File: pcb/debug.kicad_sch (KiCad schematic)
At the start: 9 parts, among them J5 TC2030, J6 CNC_Tech_3220-14-0100-00

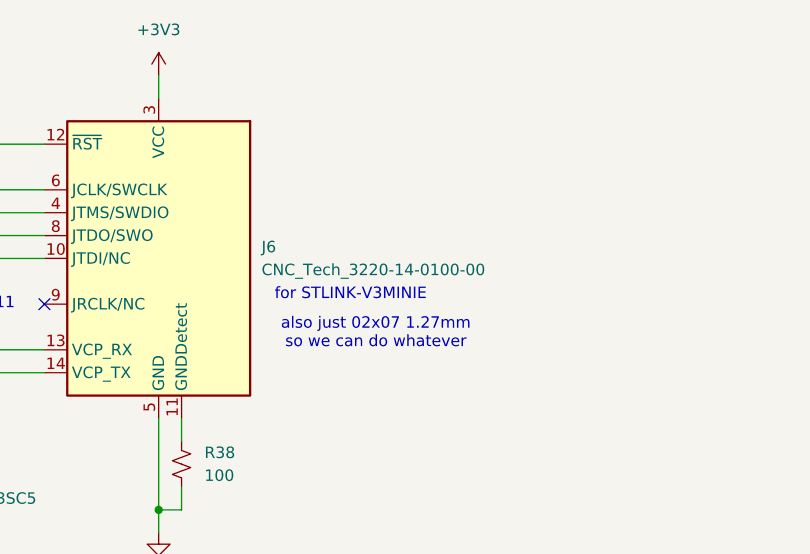
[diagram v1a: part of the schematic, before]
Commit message: Add MPN field for components except resistors
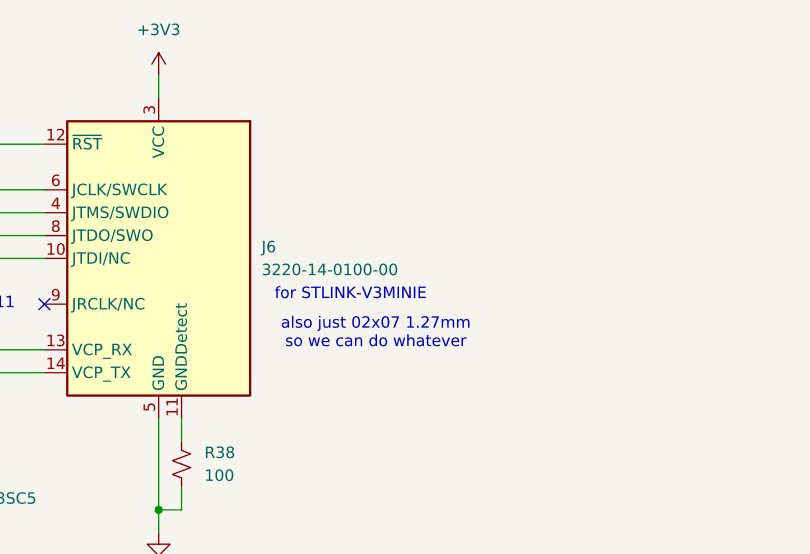
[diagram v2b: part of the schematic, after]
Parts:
- D6, D7: MPN (none) -> ESDA5V3SC5
- J6: value CNC_Tech_3220-14-0100-00 -> 3220-14-0100-00; MPN (none) -> 3220-14-0100-00
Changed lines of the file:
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@@
 			)
 		)
-		(property "Value" "CNC_Tech_3220-14-0100-00"
+		(property "Value" "3220-14-0100-00"
 			(at 125.73 44.4499 0)
 			(effects
@@
 		)
 		(property "Description" "ST Debug Connector, standard ARM Cortex-M SWD and JTAG interface plus UART"
+			(at 114.3 43.18 0)
+			(effects
+				(font
+					(size 1.27 1.27)
+				)
+				(hide yes)
+			)
+		)
+		(property "MPN" "3220-14-0100-00"
 			(at 114.3 43.18 0)
 			(effects
@@
 			)
 		)
+		(property "MPN" ""
+			(at 116.84 66.04 0)
+			(effects
+				(font
+					(size 1.27 1.27)
+				)
+				(hide yes)
+			)
+		)
 		(pin "2"
 		)
@@
 			)
 		)
+		(property "MPN" ""
+			(at 45.72 152.4 0)
+			(effects
+				(font
+					(size 1.27 1.27)
+				)
+				(hide yes)
+			)
+		)
 		(pin "1"
 		)
@@
 		)
 		(property "Description" "Quad TVS Diode Array, 5.3V Standoff, 4 Channels, 400W, ±30kV, SOT-23-5"
+			(at 55.88 68.58 0)
+			(effects
+				(font
+					(size 1.27 1.27)
+				)
+				(hide yes)
+			)
+		)
+		(property "MPN" "ESDA5V3SC5"
 			(at 55.88 68.58 0)
 			(effects
@@
 			)
 		)
+		(property "MPN" ""
+			(at 45.72 165.1 0)
+			(effects
+				(font
+					(size 1.27 1.27)
+				)
+				(hide yes)
+			)
+		)
 		(pin "1"
 		)
@@
 			)
 		)
+		(property "MPN" ""
+			(at 45.72 146.05 0)
+			(effects
+				(font
+					(size 1.27 1.27)
+				)
+				(hide yes)
+			)
+		)
 		(pin "2"
 		)
@@
 			)
 		)
+		(property "MPN" ""
+			(at 45.72 158.75 0)
+			(effects
+				(font
+					(size 1.27 1.27)
+				)
+				(hide yes)
+			)
+		)
 		(pin "2"
 		)
@@
 		)
 		(property "Description" "Quad TVS Diode Array, 5.3V Standoff, 4 Channels, 400W, ±30kV, SOT-23-5"
+			(at 81.28 68.58 0)
+			(effects
+				(font
+					(size 1.27 1.27)
+				)
+				(hide yes)
+			)
+		)
+		(property "MPN" "ESDA5V3SC5"
 			(at 81.28 68.58 0)
 			(effects
@@
 			(at 107.95 172.72 0)
 			(effects
+				(font
+					(size 1.27 1.27)
+				)
+				(hide yes)
+			)
+		)
+		(property "MPN" ""
+			(at 107.95 172.72 0)
+			(effects

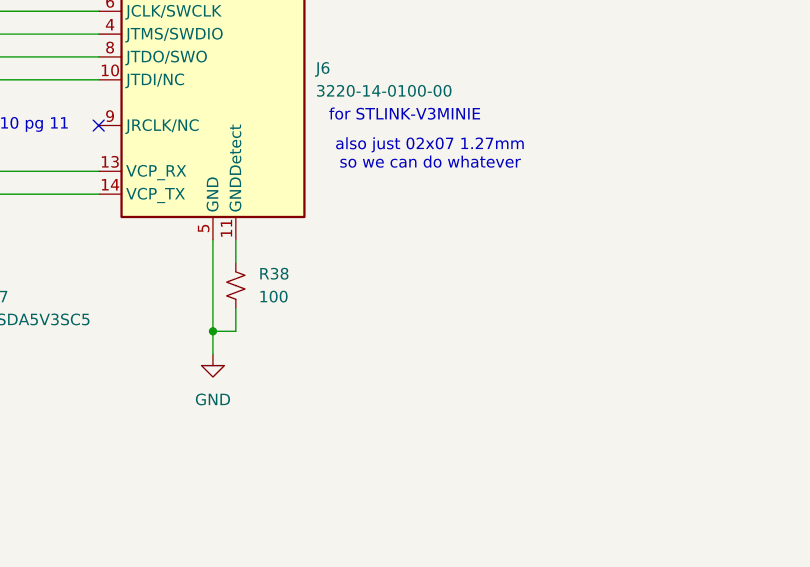
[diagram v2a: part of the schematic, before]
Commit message: BOM optimize 100 ohm resistors to 150 ohm
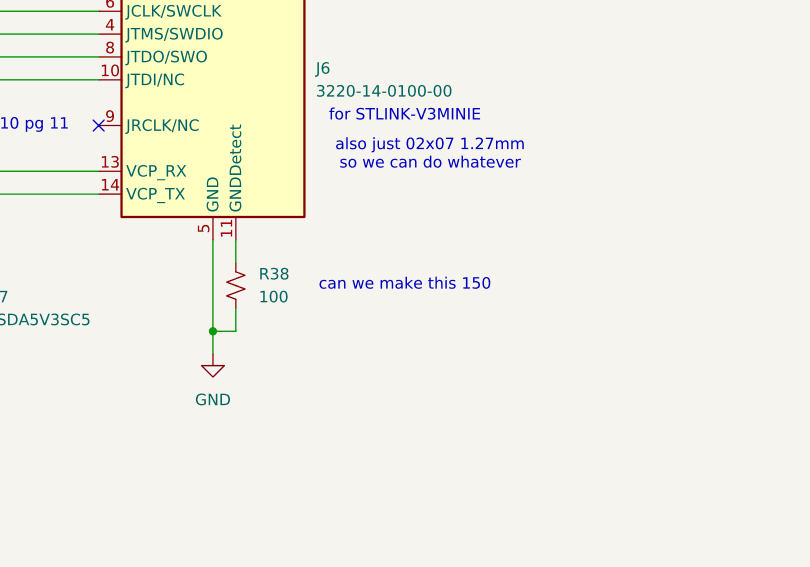
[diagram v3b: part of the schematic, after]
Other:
- note added: "can we make this 150"
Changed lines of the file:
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@@
+		)
+	)
+	(text "can we make this 150"
+		(exclude_from_sim no)
+		(at 135.636 66.04 0)
+		(effects
+			(font
+				(size 1.27 1.27)
+			)
 		)
 	)

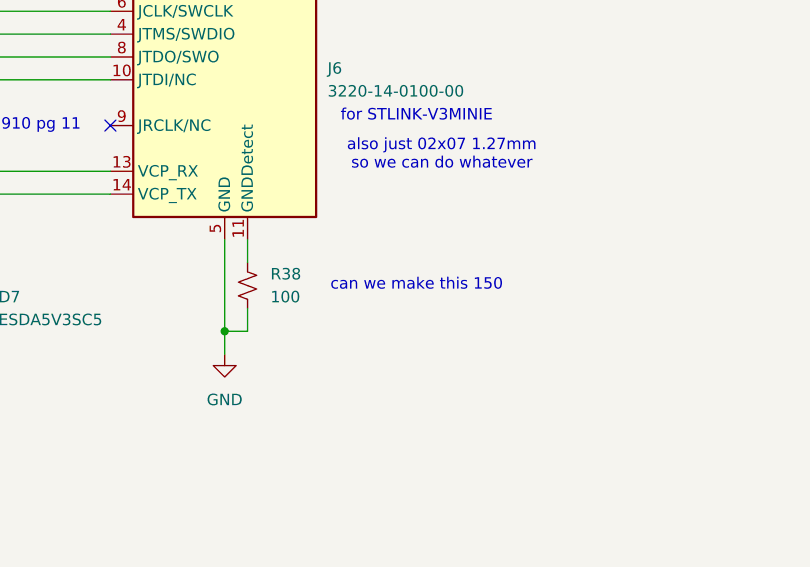
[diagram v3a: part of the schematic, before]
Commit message: BOM optimize GNDDetect 100 ohm resistor to 150 ohm
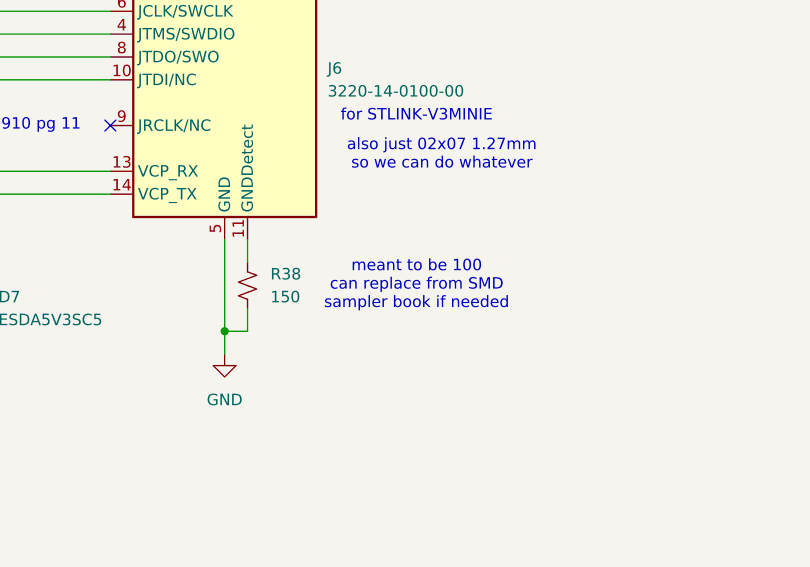
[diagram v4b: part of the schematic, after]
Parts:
- R38: value 100 -> 150
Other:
- note added: "meant to be 100 can replace from SMD sampler book if needed"
- note removed: "can we make this 150"
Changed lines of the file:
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@@
 		)
 	)
-	(text "can we make this 150"
+	(text "meant to be 100\ncan replace from SMD\nsampler book if needed"
 		(exclude_from_sim no)
 		(at 135.636 66.04 0)
@@
 			)
 		)
-		(property "Value" "100"
+		(property "Value" "150"
 			(at 119.38 67.3099 0)
 			(effects

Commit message: Update resistor MPNs
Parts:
- R38: MPN (none) -> RC0603JR-07150RL
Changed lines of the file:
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@@
 			)
 		)
-		(property "MPN" ""
+		(property "MPN" "RC0603JR-07150RL"
 			(at 116.84 66.04 0)
 			(effects

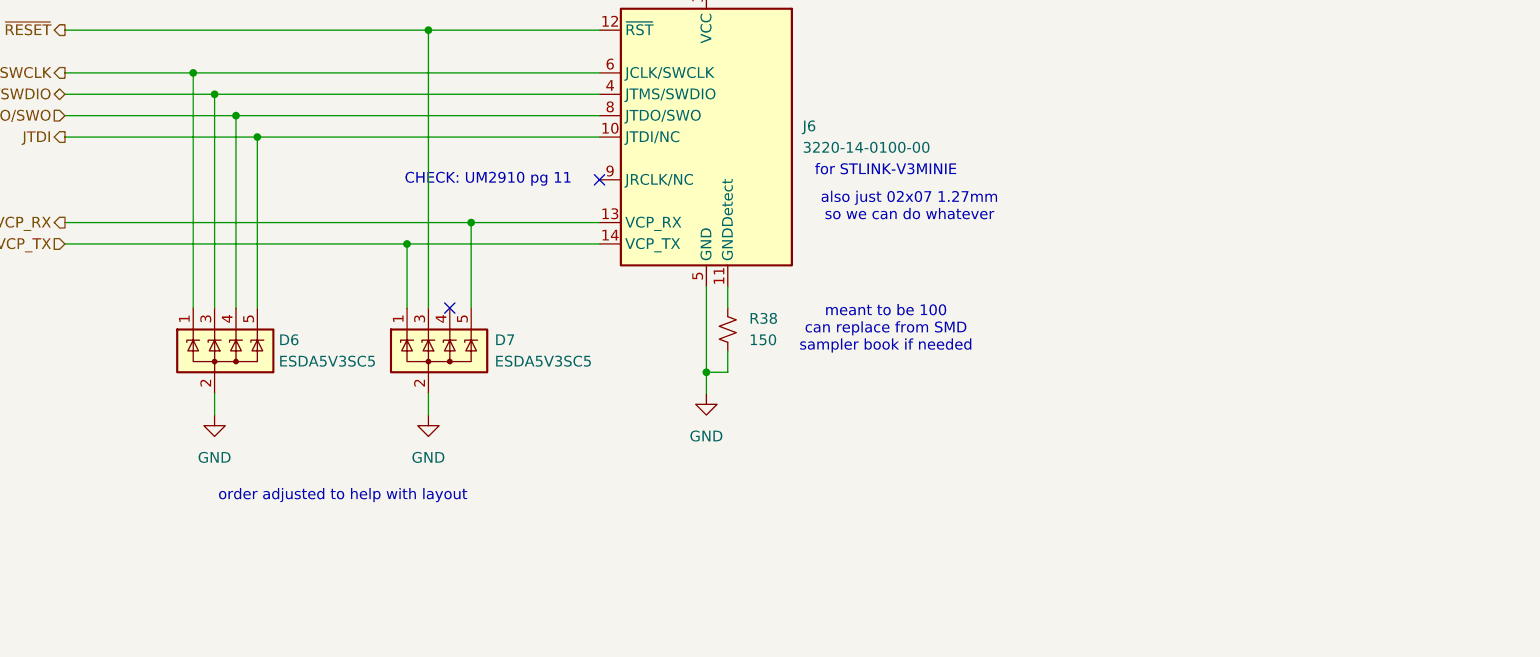
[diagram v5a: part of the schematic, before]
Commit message: Cleanup alex black eyes page
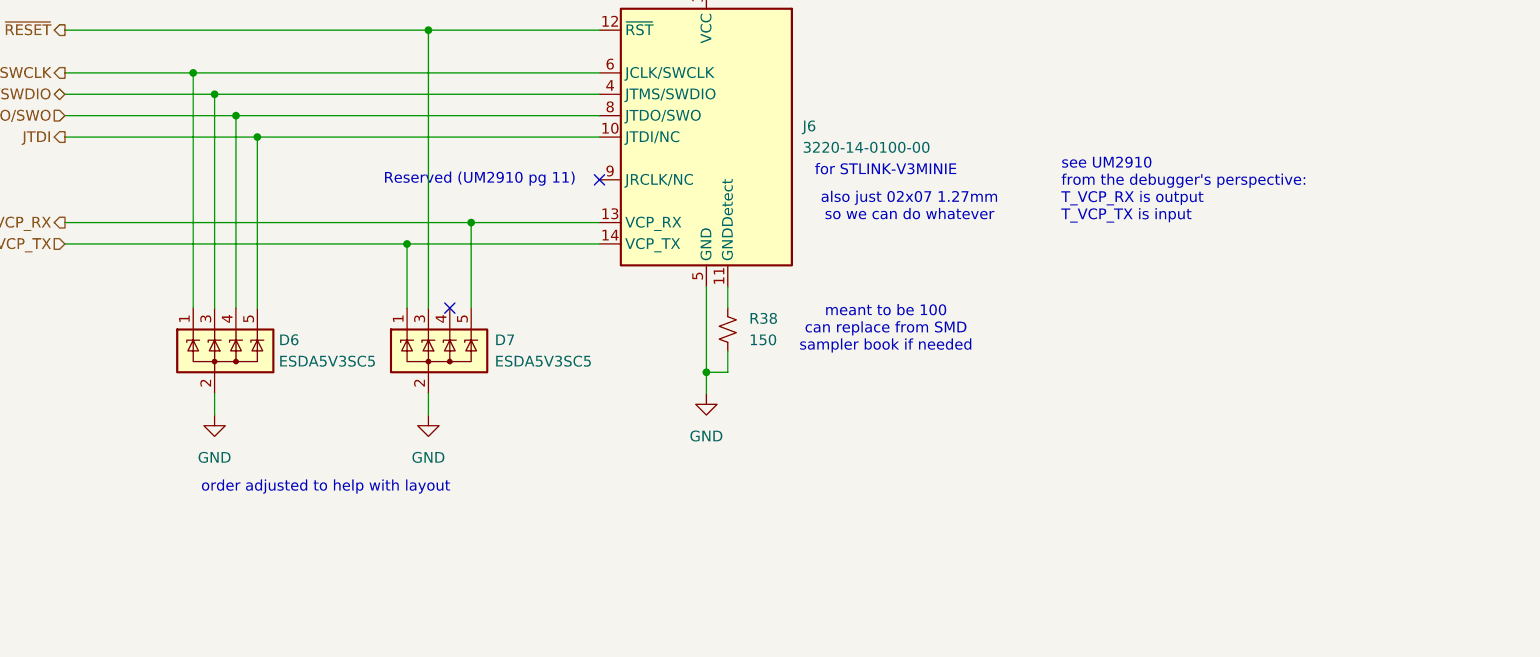
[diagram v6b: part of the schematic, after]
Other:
- note added: "Reserved (UM2910 pg 11)"
- note added: "see UM2910 from the debugger's perspective: T_VCP_RX is output T_VCP_TX is input"
- note removed: "CHECK: UM2910 pg 11"
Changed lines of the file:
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@@
 	(text "order adjusted to help with layout"
 		(exclude_from_sim no)
-		(at 71.12 85.852 0)
+		(at 69.088 84.836 0)
 		(effects
 			(font
 				(size 1.27 1.27)
 			)
+		)
+	)
+	(text "see UM2910\nfrom the debugger's perspective:\nT_VCP_RX is output\nT_VCP_TX is input"
+		(exclude_from_sim no)
+		(at 156.464 45.72 0)
+		(effects
+			(font
+				(size 1.27 1.27)
+			)
+			(justify left top)
 		)
 	)
@@
 		)
 	)
-	(text "CHECK: UM2910 pg 11"
+	(text "Reserved (UM2910 pg 11)"
 		(exclude_from_sim no)
-		(at 88.392 48.26 0)
+		(at 87.376 48.26 0)
 		(effects
 			(font

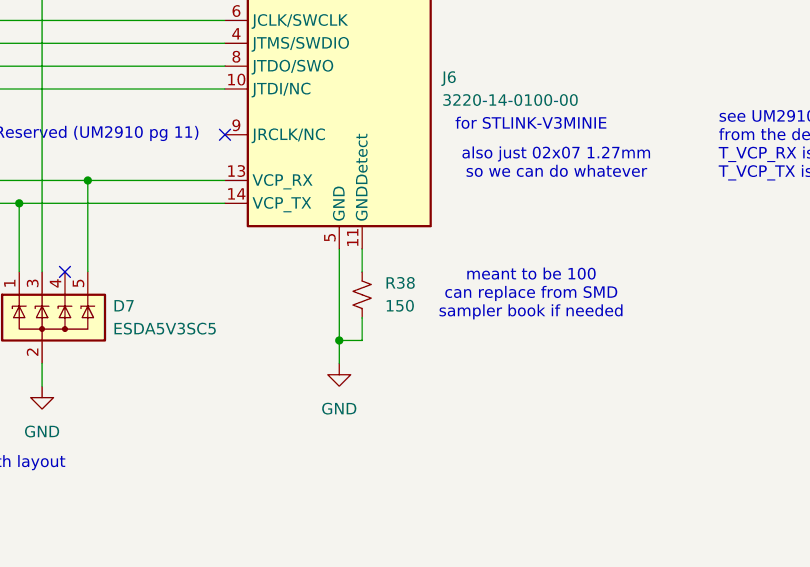
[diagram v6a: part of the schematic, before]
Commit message: Redo layout and routing for RGB LEDs
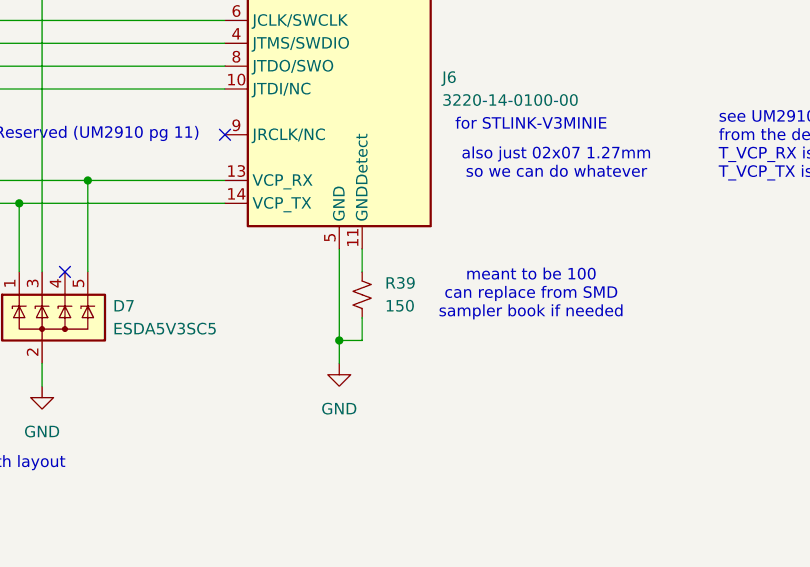
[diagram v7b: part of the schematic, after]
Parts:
- renumbered R38 to R39

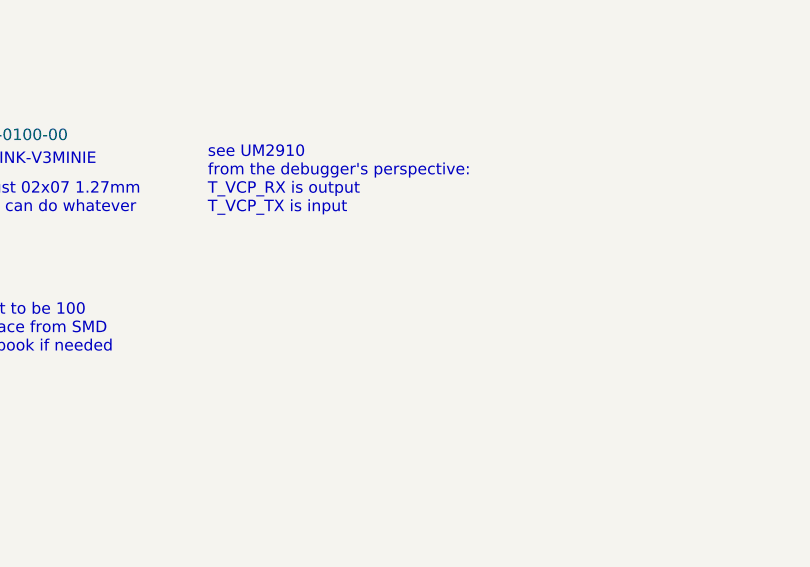
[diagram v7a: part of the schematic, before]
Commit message: Plot schematics for tech report
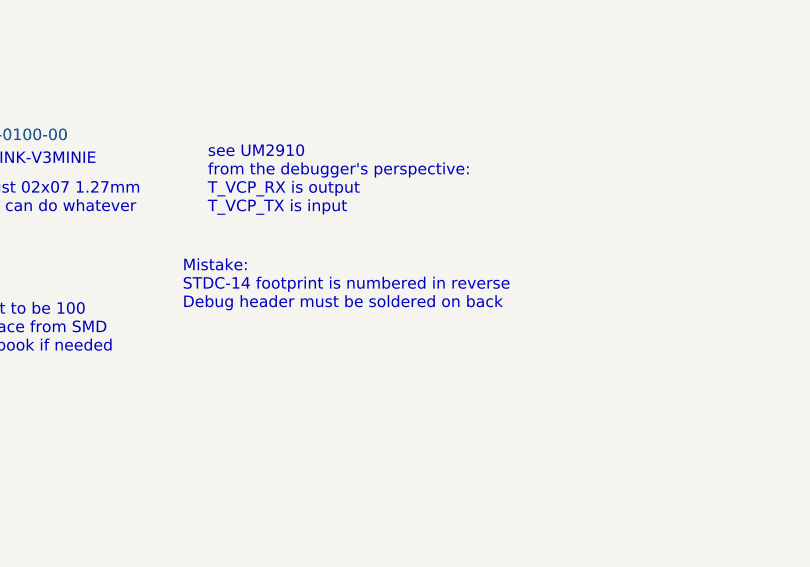
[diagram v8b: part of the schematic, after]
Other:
- note added: "Mistake: STDC-14 footprint is numbered in reverse Debug header must be soldered on back"
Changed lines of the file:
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@@
+		)
+	)
+	(text "Mistake:\nSTDC-14 footprint is numbered in reverse\nDebug header must be soldered on back"
+		(exclude_from_sim no)
+		(at 153.67 58.42 0)
+		(effects
+			(font
+				(size 1.27 1.27)
+				(color 255 0 0 1)
+			)
+			(justify left top)
 		)
 	)
